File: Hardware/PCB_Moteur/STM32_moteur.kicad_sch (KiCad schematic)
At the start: 58 parts, among them J2 Conn_01x06_Pin, U1 STM32F103CBT6

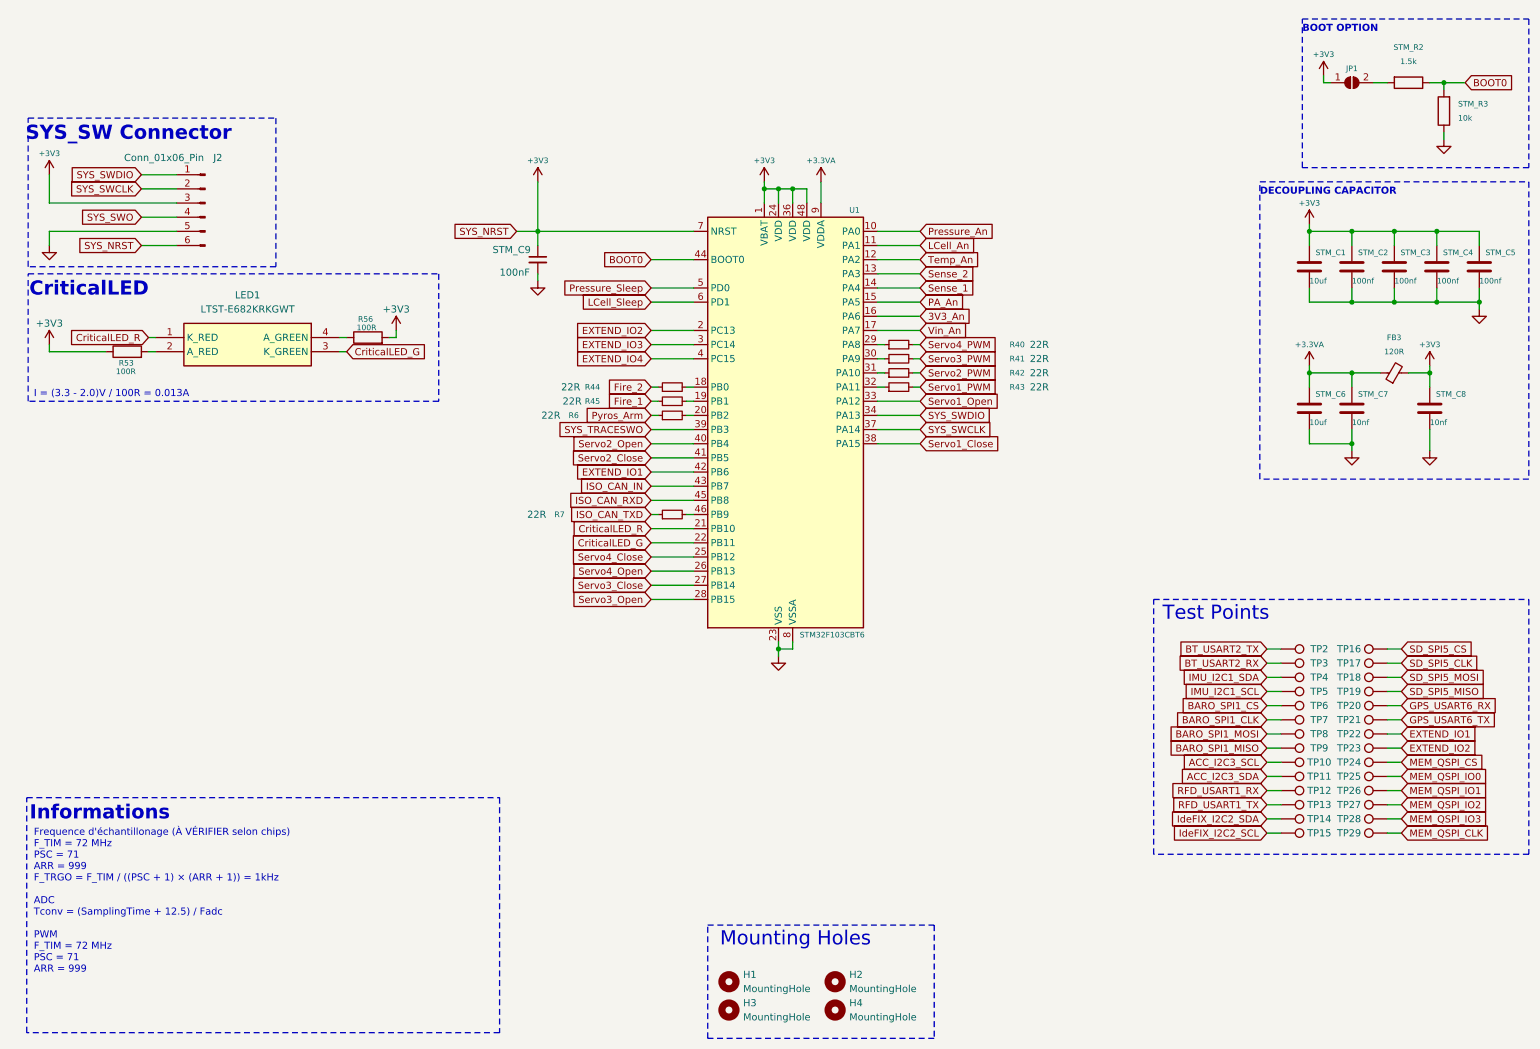
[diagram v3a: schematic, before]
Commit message: fix: LDO 5V SHDN + REFs (missing) + change EN valves controller connection + fix intrumental ampliop + add pull-down to sleep pins
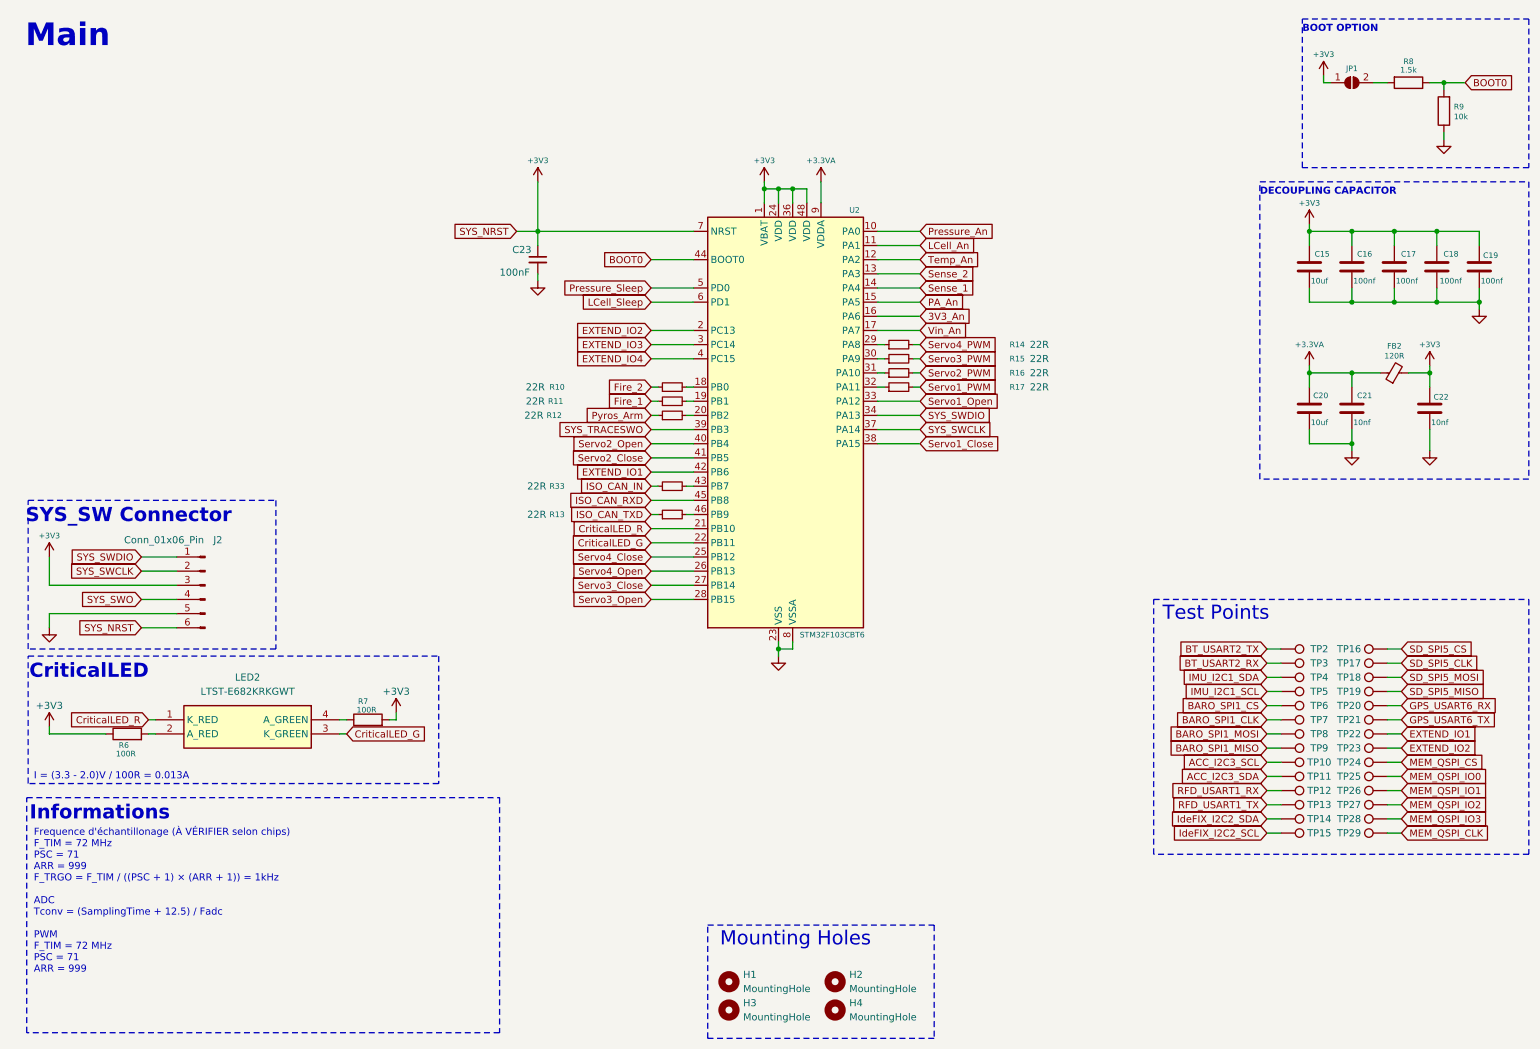
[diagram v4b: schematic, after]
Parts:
- added R33: 22R, Resistor_SMD:R_0603_1608Metric, symbol Device:R_Small
- renumbered STM_C1 to C15, STM_C2 to C16, STM_C3 to C17, STM_C4 to C18, STM_C5 to C19, STM_C6 to C20, STM_C7 to C21, STM_C8 to C22, STM_C9 to C23, FB3 to FB2, LED1 to LED2, R44 to R10, R45 to R11, R6 to R12, R7 to R13, R40 to R14, R41 to R15, R42 to R16, R43 to R17, R53 to R6, R56 to R7, STM_R2 to R8, STM_R3 to R9, U1 to U2
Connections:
- net ISO_CAN_IN: now also R33.1; no longer U2.43 (PB7)
- new net: R33.2, U2.43 (PB7)
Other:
- note added: "Main"
- moved on the sheet: J2, LED2, R6, R7

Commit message: wip : minor corrections and fix footprints except connectors
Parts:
- C23: footprint Capacitor_SMD:C_0603_1608Metric -> Capacitor_SMD:C_0805_2012Metric
- H1, H2, H3, H4: footprint (none) -> MountingHole:MountingHole_4.3mm_M4
- LED2: footprint LTSTE683RGBW -> pcb_moteur:LTSTE683RGBW
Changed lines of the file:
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@@
 			)
 		)
-		(property "Footprint" ""
+		(property "Footprint" "MountingHole:MountingHole_4.3mm_M4"
 			(at 139.7 186.69 0)
 			(effects
@@
 			)
 		)
-		(property "Footprint" "Capacitor_SMD:C_0603_1608Metric"
+		(property "Footprint" "Capacitor_SMD:C_0805_2012Metric"
 			(at 105.41 57.15 0)
 			(effects
@@
 			)
 		)
-		(property "Footprint" ""
+		(property "Footprint" "MountingHole:MountingHole_4.3mm_M4"
 			(at 158.75 186.69 0)
 			(effects
@@
 			)
 		)
-		(property "Footprint" ""
+		(property "Footprint" "MountingHole:MountingHole_4.3mm_M4"
 			(at 158.75 191.77 0)
 			(effects
@@
 			)
 		)
-		(property "Footprint" "LTSTE683RGBW"
+		(property "Footprint" "pcb_moteur:LTSTE683RGBW"
 			(at 40.64 234.62 0)
 			(effects
@@
 			)
 		)
-		(property "Footprint" ""
+		(property "Footprint" "MountingHole:MountingHole_4.3mm_M4"
 			(at 139.7 191.77 0)
 			(effects

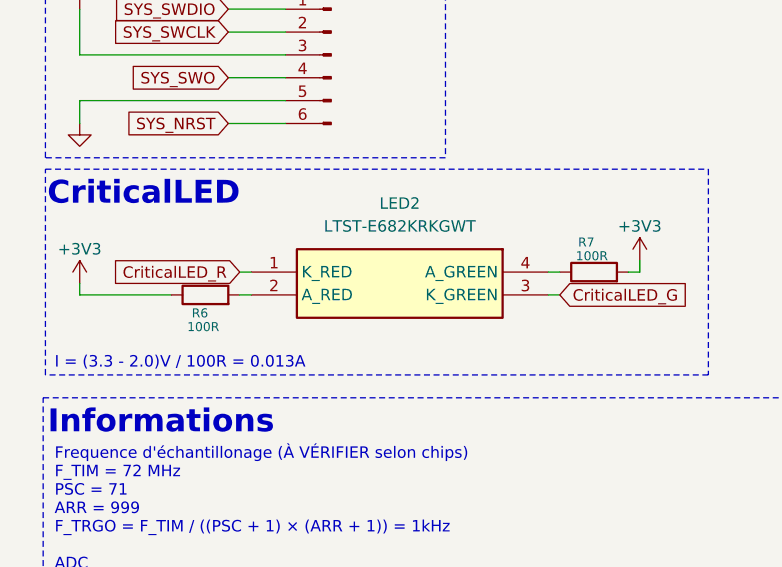
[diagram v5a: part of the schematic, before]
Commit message: fix: symbols refactorisation (footprint missing)
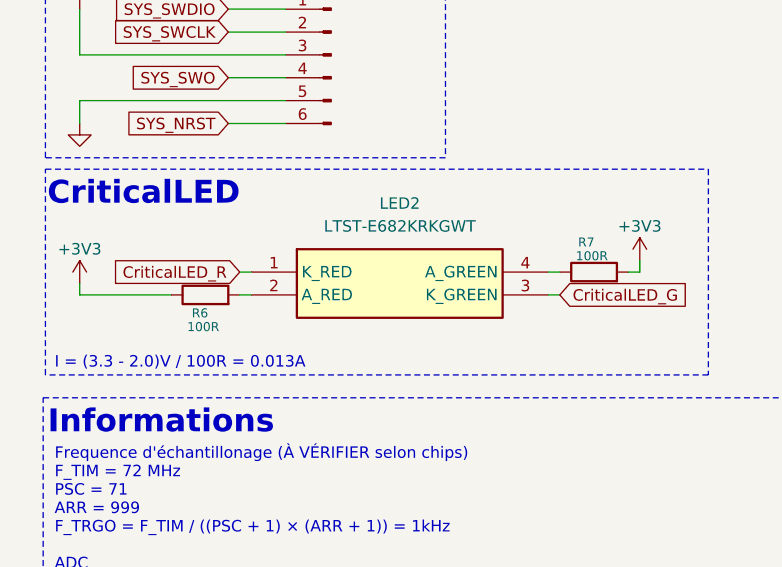
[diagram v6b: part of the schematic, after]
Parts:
- LED2: footprint pcb_moteur:LTSTE683RGBW -> LTSTE683RGBW
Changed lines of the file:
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@@
-	)
-	(symbol
-		(lib_id "pcb_moteur:LTST-E682KRKGWT")
-		(at 69.85 139.7 0)
-		(mirror y)
-		(unit 1)
-		(exclude_from_sim no)
-		(in_bom yes)
-		(on_board yes)
-		(dnp no)
-		(property "Reference" "LED2"
-			(at 53.34 132.08 0)
-			(effects
-				(font
-					(size 1.27 1.27)
-				)
-			)
-		)
-		(property "Value" "LTST-E682KRKGWT"
-			(at 53.34 134.62 0)
-			(effects
-				(font
-					(size 1.27 1.27)
-				)
-			)
-		)
-		(property "Footprint" "pcb_moteur:LTSTE683RGBW"
-			(at 40.64 234.62 0)
-			(effects
-				(font
-					(size 1.27 1.27)
-				)
-				(justify left top)
-				(hide yes)
-			)
-		)
-		(property "Datasheet" "https://optoelectronics.liteon.com/upload/download/DS22-2011-0354/LTST-E682KRKGWT.pdf"
-			(at 40.64 334.62 0)
-			(effects
-				(font
-					(size 1.27 1.27)
-				)
-				(justify left top)
-				(hide yes)
-			)
-		)
-		(property "Description" "Red/Yell-Green LED SMD PLCC4 637/569nm"
-			(at 69.85 139.7 0)
-			(effects
-				(font
-					(size 1.27 1.27)
-				)
-				(hide yes)
-			)
-		)
-		(property "Height" "2"
-			(at 40.64 534.62 0)
-			(effects
-				(font
-					(size 1.27 1.27)
-				)
-				(justify left top)
-				(hide yes)
-			)
-		)
-		(property "Mouser Part Number" "859-LTST-E682KRKGWT"
-			(at 40.64 634.62 0)
-			(effects
-				(font
-					(size 1.27 1.27)
-				)
-				(justify left top)
-				(hide yes)
-			)
-		)
-		(property "Mouser Price/Stock" "https://www.mouser.co.uk/ProductDetail/Lite-On/LTST-E682KRKGWT?qs=xb8aMrBSZRL4Mm2v%2F2Q1nw%3D%3D"
-			(at 40.64 734.62 0)
-			(effects
-				(font
-					(size 1.27 1.27)
-				)
-				(justify left top)
-				(hide yes)
-			)
-		)
-		(property "Manufacturer_Name" "Lite-On"
-			(at 40.64 834.62 0)
-			(effects
-				(font
-					(size 1.27 1.27)
-				)
-				(justify left top)
-				(hide yes)
-			)
-		)
-		(property "Manufacturer_Part_Number" "LTST-E682KRKGWT"
-			(at 40.64 934.62 0)
-			(effects
-				(font
-					(size 1.27 1.27)
-				)
-				(justify left top)
-				(hide yes)
-			)
-		)
-		(pin "4"
-		)
-		(pin "3"
-		)
-		(pin "1"
-		)
-		(pin "2"
-		)
-		(instances
-			(project ""
-				(path "/b0d87684-7b1c-41d8-8358-755aa327573e/753d1783-c2f5-4012-bbb8-3f4eadf066f6"
-					(reference "LED2")
-					(unit 1)
-				)
-			)
-		)
 	)
 	(symbol
@@
 					(unit 1)
 				)
+			)
+		)
+	)
+	(symbol
+		(lib_id "pcb_moteur:LTST-E682KRKGWT")
+		(at 36.83 139.7 0)
+		(unit 1)
+		(exclude_from_sim no)
+		(in_bom yes)
+		(on_board yes)
+		(dnp no)
+		(fields_autoplaced yes)
+		(property "Reference" "LED2"
+			(at 53.34 132.08 0)
+			(effects
+				(font
+					(size 1.27 1.27)
+				)
+			)
+		)
+		(property "Value" "LTST-E682KRKGWT"
+			(at 53.34 134.62 0)
+			(effects
+				(font
+					(size 1.27 1.27)
+				)
+			)
+		)
+		(property "Footprint" "LTSTE683RGBW"
+			(at 66.04 234.62 0)
+			(effects
+				(font
+					(size 1.27 1.27)
+				)
+				(justify left top)
+				(hide yes)
+			)
+		)
+		(property "Datasheet" "https://optoelectronics.liteon.com/upload/download/DS22-2011-0354/LTST-E682KRKGWT.pdf"
+			(at 66.04 334.62 0)
+			(effects
+				(font
+					(size 1.27 1.27)
+				)
+				(justify left top)
+				(hide yes)
+			)
+		)
+		(property "Description" "Red/Yell-Green LED SMD PLCC4 637/569nm"
+			(at 36.83 139.7 0)
+			(effects
+				(font
+					(size 1.27 1.27)
+				)
+				(hide yes)
+			)
+		)
+		(property "Height" "2"
+			(at 66.04 534.62 0)
+			(effects
+				(font
+					(size 1.27 1.27)
+				)
+				(justify left top)
+				(hide yes)
+			)
+		)
+		(property "Mouser Part Number" "859-LTST-E682KRKGWT"
+			(at 66.04 634.62 0)
+			(effects
+				(font
+					(size 1.27 1.27)
+				)
+				(justify left top)
+				(hide yes)
+			)
+		)
+		(property "Mouser Price/Stock" "https://www.mouser.co.uk/ProductDetail/Lite-On/LTST-E682KRKGWT?qs=xb8aMrBSZRL4Mm2v%2F2Q1nw%3D%3D"
+			(at 66.04 734.62 0)
+			(effects
+				(font
+					(size 1.27 1.27)
+				)
+				(justify left top)
+				(hide yes)
+			)
+		)
+		(property "Manufacturer_Name" "Lite-On"
+			(at 66.04 834.62 0)
+			(effects
+				(font
+					(size 1.27 1.27)
+				)
+				(justify left top)
+				(hide yes)
+			)
+		)
+		(property "Manufacturer_Part_Number" "LTST-E682KRKGWT"
+			(at 66.04 934.62 0)
+			(effects
+				(font
+					(size 1.27 1.27)
+				)
+				(justify left top)
+				(hide yes)
+			)
+		)
+		(pin "2"
+		)
+		(pin "4"
+		)
+		(pin "1"
+		)
+		(pin "3"
+		)
+		(instances
+			(project ""
+				(path "/b0d87684-7b1c-41d8-8358-755aa327573e/753d1783-c2f5-4012-bbb8-3f4eadf066f6"
+					(reference "LED2")
+					(unit 1)
+				)

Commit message: wip : done all footprints
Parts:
- C15, C20: value 10uf -> 10uF
- C16, C17, C18, C19: value 100nf -> 100nF
- C21, C22: value 10nf -> 10nF
- J2: footprint (none) -> Connector_PinHeader_2.54mm:PinHeader_1x06_P2.54mm_Vertical
- LED2: footprint LTSTE683RGBW -> pcb_moteur:LTSTE683RGBW
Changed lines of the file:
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@@
 			)
 		)
-		(property "Value" "100nf"
+		(property "Value" "100nF"
 			(at 259.334 60.96 0)
 			(effects
@@
 			)
 		)
-		(property "Value" "10nf"
+		(property "Value" "10nF"
 			(at 251.714 86.36 0)
 			(effects
@@
 			)
 		)
-		(property "Footprint" ""
+		(property "Footprint" "Connector_PinHeader_2.54mm:PinHeader_1x06_P2.54mm_Vertical"
 			(at 45.72 115.57 0)
 			(effects
@@
 			)
 		)
-		(property "Value" "10nf"
+		(property "Value" "10nF"
 			(at 265.684 86.36 0)
 			(effects
@@
 			)
 		)
-		(property "Value" "100nf"
+		(property "Value" "100nF"
 			(at 267.208 60.96 0)
 			(effects
@@
 			)
 		)
-		(property "Value" "100nf"
+		(property "Value" "100nF"
 			(at 274.574 60.96 0)
 			(effects
@@
 			)
 		)
-		(property "Footprint" "LTSTE683RGBW"
+		(property "Footprint" "pcb_moteur:LTSTE683RGBW"
 			(at 66.04 234.62 0)
 			(effects
@@
 			)
 		)
-		(property "Value" "10uf"
+		(property "Value" "10uF"
 			(at 244.094 60.96 0)
 			(effects
@@
 			)
 		)
-		(property "Value" "10uf"
+		(property "Value" "10uF"
 			(at 244.094 86.36 0)
 			(effects
@@
 			)
 		)
-		(property "Value" "100nf"
+		(property "Value" "100nF"
 			(at 251.714 60.96 0)
 			(effects

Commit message: wip: layout circuits Pyro
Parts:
- R10, R11, R12, R13, R14, R15, R16, R17, R33, R6, R7: footprint Resistor_SMD:R_0603_1608Metric -> Resistor_SMD:R_0805_2012Metric
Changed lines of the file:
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@@
 			)
 		)
-		(property "Footprint" "Resistor_SMD:R_0603_1608Metric"
+		(property "Footprint" "Resistor_SMD:R_0805_2012Metric"
 			(at 170.18 74.93 0)
 			(effects
@@
 			)
 		)
-		(property "Footprint" "Resistor_SMD:R_0603_1608Metric"
+		(property "Footprint" "Resistor_SMD:R_0805_2012Metric"
 			(at 74.93 141.478 90)
 			(effects
@@
 			)
 		)
-		(property "Footprint" "Resistor_SMD:R_0603_1608Metric"
+		(property "Footprint" "Resistor_SMD:R_0805_2012Metric"
 			(at 129.54 80.01 0)
 			(effects
@@
 			)
 		)
-		(property "Footprint" "Resistor_SMD:R_0603_1608Metric"
+		(property "Footprint" "Resistor_SMD:R_0805_2012Metric"
 			(at 129.54 97.79 0)
 			(effects
@@
 			)
 		)
-		(property "Footprint" "Resistor_SMD:R_0603_1608Metric"
+		(property "Footprint" "Resistor_SMD:R_0805_2012Metric"
 			(at 170.18 72.39 0)
 			(effects
@@
 			)
 		)
-		(property "Footprint" "Resistor_SMD:R_0603_1608Metric"
+		(property "Footprint" "Resistor_SMD:R_0805_2012Metric"
 			(at 170.18 77.47 0)
 			(effects
@@
 			)
 		)
-		(property "Footprint" "Resistor_SMD:R_0603_1608Metric"
+		(property "Footprint" "Resistor_SMD:R_0805_2012Metric"
 			(at 129.54 85.09 0)
 			(effects
@@
 			)
 		)
-		(property "Footprint" "Resistor_SMD:R_0603_1608Metric"
+		(property "Footprint" "Resistor_SMD:R_0805_2012Metric"
 			(at 170.18 80.01 0)
 			(effects
@@
 			)
 		)
-		(property "Footprint" "Resistor_SMD:R_0603_1608Metric"
+		(property "Footprint" "Resistor_SMD:R_0805_2012Metric"
 			(at 129.54 82.55 0)
 			(effects
@@
 			)
 		)
-		(property "Footprint" "Resistor_SMD:R_0603_1608Metric"
+		(property "Footprint" "Resistor_SMD:R_0805_2012Metric"
 			(at 31.75 144.018 90)
 			(effects
@@
 			)
 		)
-		(property "Footprint" "Resistor_SMD:R_0603_1608Metric"
+		(property "Footprint" "Resistor_SMD:R_0805_2012Metric"
 			(at 129.54 102.87 0)
 			(effects
